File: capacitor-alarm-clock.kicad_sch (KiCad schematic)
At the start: 0 parts

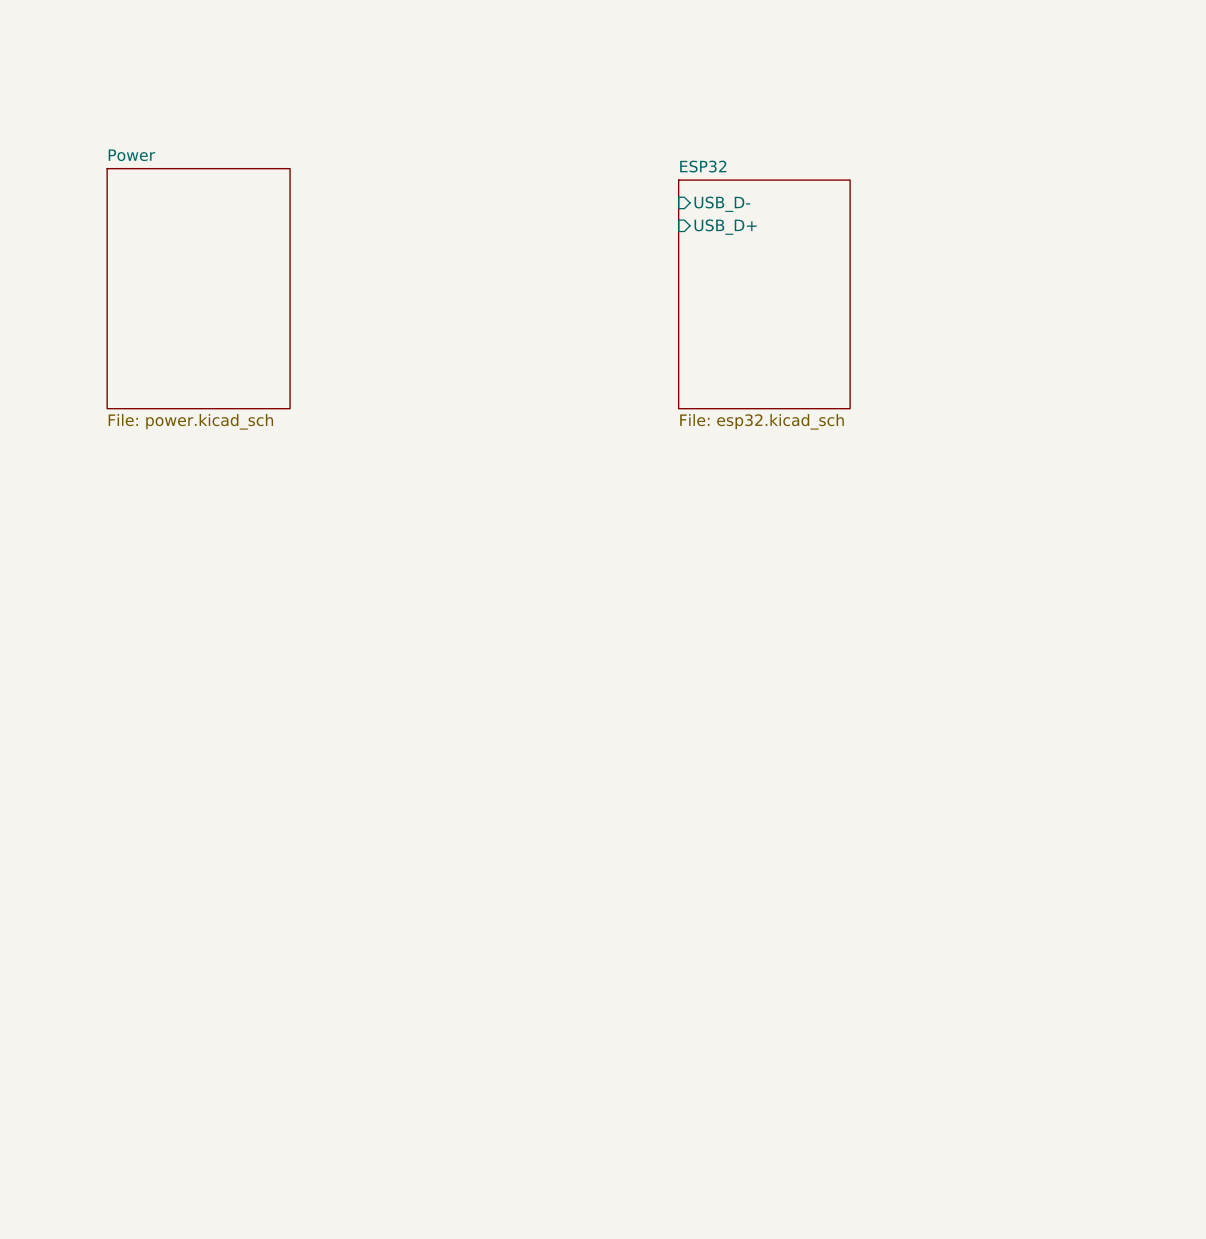
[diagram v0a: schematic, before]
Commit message: Finished the power, USB and ESP32 parts of the schematic
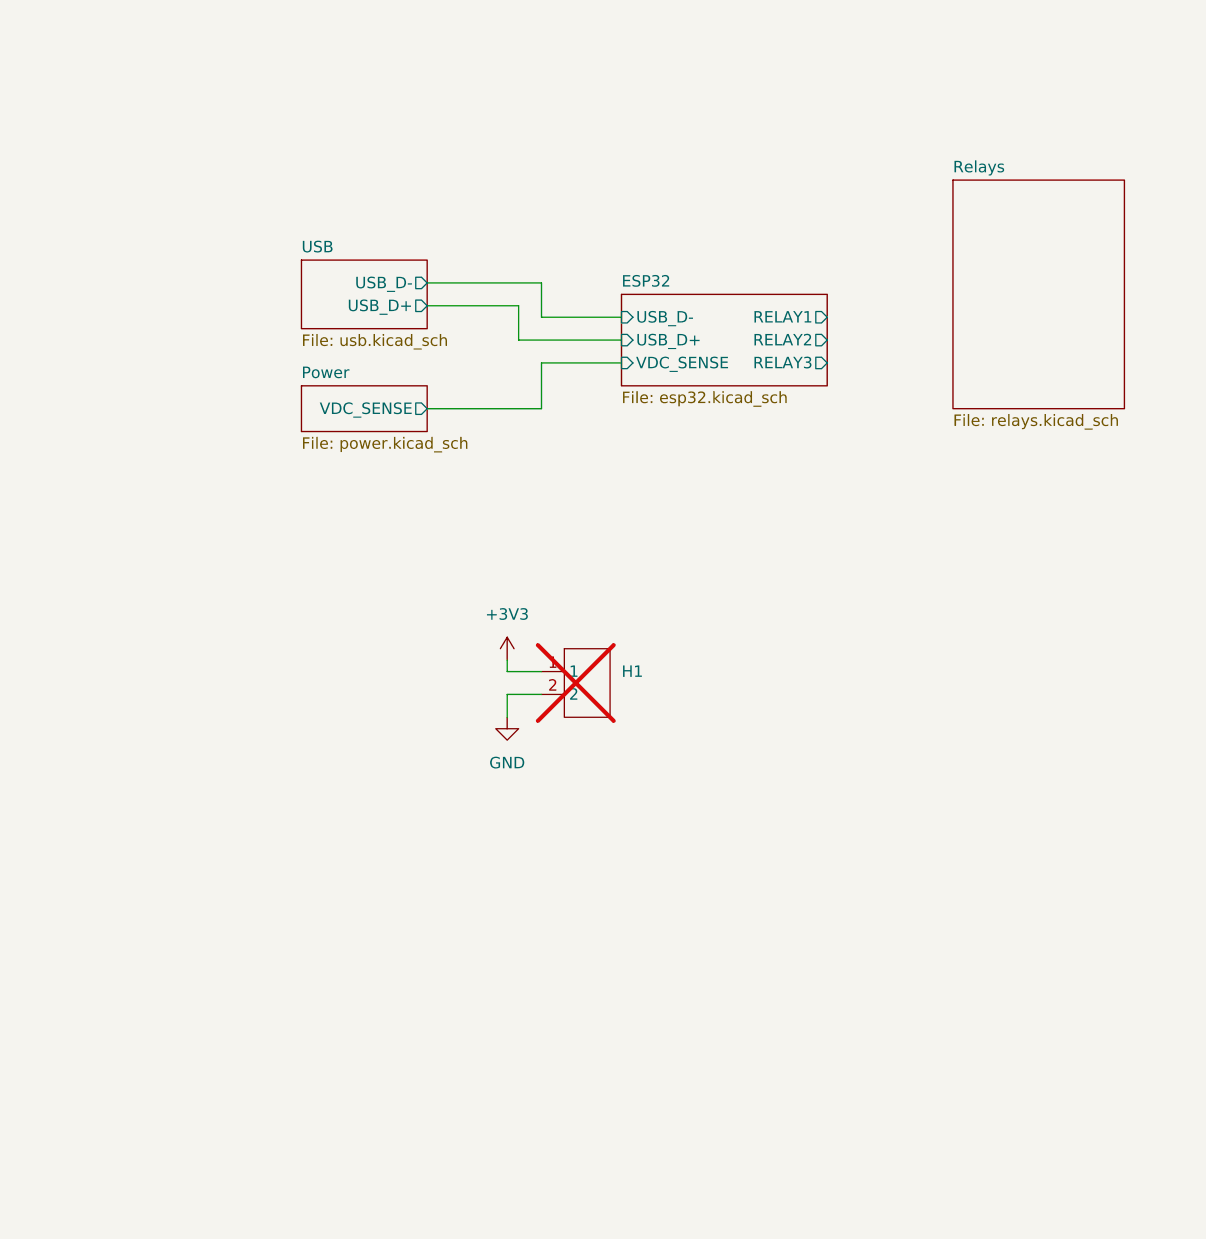
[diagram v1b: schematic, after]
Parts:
- added H1: ~, EasyEDA_Lib:HDR-TH_2P-P2.54-V-M, symbol EasyEDA_Lib:PZ254V-11-02P
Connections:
- new net +3V3: H1.1
- new net GND: H1.2
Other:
- added sheet Relays (relays.kicad_sch)
- added sheet USB (usb.kicad_sch)
- sheet ESP32 ports: added RELAY1, RELAY2, RELAY3, VDC_SENSE; removed none
- sheet Power ports: added VDC_SENSE; removed none

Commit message: Finished schematics, started component placement
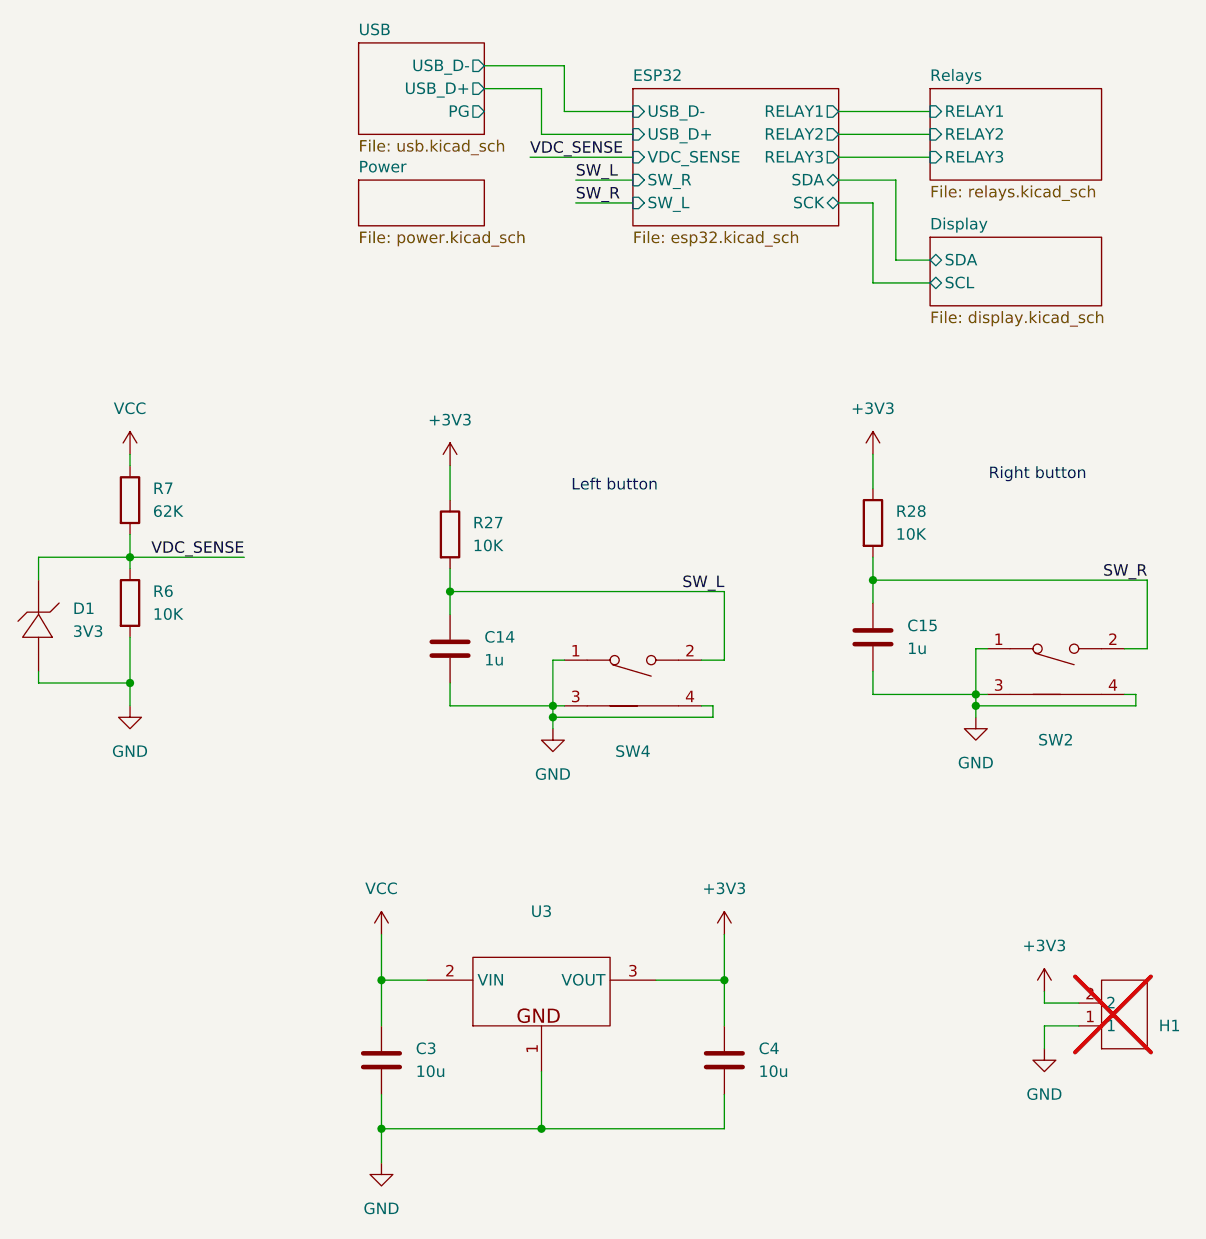
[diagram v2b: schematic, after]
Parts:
- added C14, C15: 1u, Capacitor_SMD:C_0603_1608Metric, symbol Device:C
- added C3, C4: 10u, Capacitor_SMD:C_0603_1608Metric, symbol Device:C
- added D1: 3V3, EasyEDA_Lib:SOD-123_L2.7-W1.6-LS3.7-RD, symbol EasyEDA_Lib:BZT52C3V3
- added R27, R28, R6: 10K, Resistor_SMD:R_0603_1608Metric, symbol Device:R
- added R7: 62K, Resistor_SMD:R_0603_1608Metric, symbol Device:R
- added SW2, SW4: ~, EasyEDA_Lib:SW-TH_TS665ZJ, symbol EasyEDA_Lib:TS665ZJ
- added U3: ~, EasyEDA_Lib:SOT-89-3_L4.5-W2.5-P1.50-LS4.2-BR, symbol EasyEDA_Lib:HT7333-1-MS_C7434186
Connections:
- net +3V3: now also H1.2, C4.1, R27.1, R28.1, U3.3 (VOUT); no longer H1.1
- net GND: now also H1.1, C14.2, C15.2, C3.2, C4.2, D1.2 (A), R6.2, SW2.1, SW2.3, SW2.4, SW4.1, SW4.3, SW4.4, U3.1 (GND); no longer H1.2
- new net SW_L: C14.1, R27.2, SW4.2
- new net SW_R: C15.1, R28.2, SW2.2
- new net VCC: C3.1, R7.1, U3.2 (VIN)
- new net VDC_SENSE: D1.1 (K), R6.1, R7.2
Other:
- added sheet Display (display.kicad_sch)
- sheet ESP32 ports: added SCK, SDA, SW_L, SW_R; removed none
- sheet Power ports: added none; removed VDC_SENSE
- sheet Relays ports: added RELAY1, RELAY2, RELAY3; removed none
- sheet USB ports: added PG; removed none
- note added: "Left button"
- note added: "Right button"
- moved on the sheet: H1
